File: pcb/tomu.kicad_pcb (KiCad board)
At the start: 2 copper layers, 13.2 x 10 mm, 16 parts, among them P1 USART0, P2 DEBUG, P3 USB-PCB, P4 RESET_PAD, P5 5V_PAD, P6 3V_PAD, U1 EFM32HG309

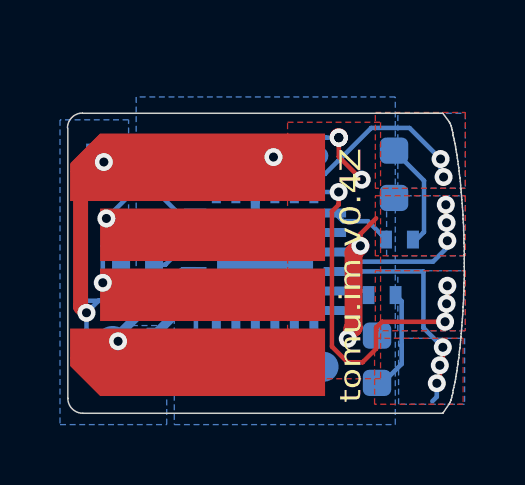
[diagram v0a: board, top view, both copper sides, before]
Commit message: eliminate edge.cut DRC
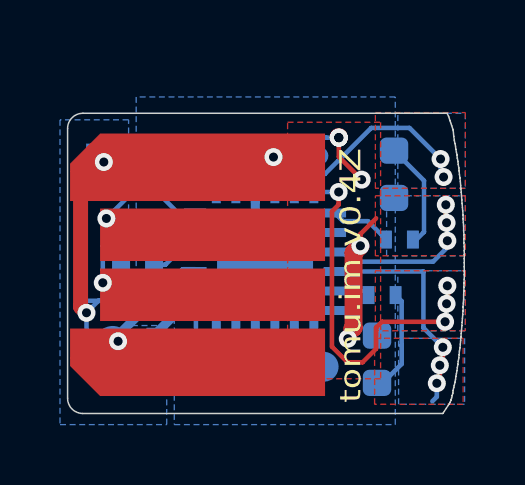
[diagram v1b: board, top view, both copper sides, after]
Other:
- outline, holes or cut-outs redrawn
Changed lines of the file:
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@@
 (kicad_pcb (version 20211014) (generator pcbnew)
   (general
-    (thickness 0.6)
+    (thickness 1.6)
   )
   (paper "User" 200 150.012)
@@
   )
   (setup
+    (stackup
+      (layer "F.SilkS" (type "Top Silk Screen"))
+      (layer "F.Paste" (type "Top Solder Paste"))
+      (layer "F.Mask" (type "Top Solder Mask") (thickness 0.01))
+      (layer "F.Cu" (type "copper") (thickness 0.035))
+      (layer "dielectric 1" (type "core") (thickness 1.51) (material "FR4") (epsilon_r 4.5) (loss_tangent 0.02))
+      (layer "B.Cu" (type "copper") (thickness 0.035))
+      (layer "B.Mask" (type "Bottom Solder Mask") (thickness 0.01))
+      (layer "B.Paste" (type "Bottom Solder Paste"))
+      (layer "B.SilkS" (type "Bottom Silk Screen"))
+      (copper_finish "None")
+      (dielectric_constraints no)
+    )
     (pad_to_mask_clearance 0.07)
     (solder_mask_min_width 0.07)
     (aux_axis_origin 17.025 26.5)
-    (grid_origin 29.12902 16.713447)
+    (grid_origin 29.717 16.8)
     (pcbplotparams
       (layerselection 0x00010fc_80000001)
@@
   (gr_line (start 29.95 17.05) (end 18.95 17.05) (layer "Dwgs.User") (width 0.1))
   (gr_line (start 18.95 26.05) (end 29.95 26.05) (layer "Dwgs.User") (width 0.1))
-  (gr_arc (start 17.012461 17.292697) (mid 17.158908 16.939144) (end 17.512461 16.792697) (layer "Edge.Cuts") (width 0.05))
-  (gr_line (start 29.888221 17.626525) (end 29.868221 17.536525) (layer "Edge.Cuts") (width 0.05))
   (gr_line (start 30.198221 20.316525) (end 30.198221 20.186525) (layer "Edge.Cuts") (width 0.05))
-  (gr_line (start 29.908221 17.706525) (end 29.888221 17.626525) (layer "Edge.Cuts") (width 0.05))
+  (gr_line locked (start 29.908221 17.706525) (end 29.888221 17.562) (layer "Edge.Cuts") (width 0.05))
   (gr_line (start 29.958221 17.996525) (end 29.948221 17.896525) (layer "Edge.Cuts") (width 0.05))
   (gr_line (start 30.218221 22.856525) (end 30.228221 22.726525) (layer "Edge.Cuts") (width 0.05))
   (gr_line (start 30.228221 22.726525) (end 30.228221 22.596525) (layer "Edge.Cuts") (width 0.05))
   (gr_line (start 29.868221 26.036525) (end 29.888221 25.946525) (layer "Edge.Cuts") (width 0.05))
+  (gr_arc (start 17.017 17.308) (mid 17.16579 16.94879) (end 17.525001 16.8) (layer "Edge.Cuts") (width 0.05))
   (gr_line (start 30.028221 18.406525) (end 30.008221 18.296525) (layer "Edge.Cuts") (width 0.05))
   (gr_line (start 30.218221 20.716525) (end 30.218221 20.576525) (layer "Edge.Cuts") (width 0.05))
   (gr_line (start 30.108221 24.496525) (end 30.118221 24.376525) (layer "Edge.Cuts") (width 0.05))
+  (gr_line (start 29.8186 17.2064) (end 29.7678 17.054) (layer "Edge.Cuts") (width 0.05))
   (gr_line (start 30.208221 23.126525) (end 30.218221 22.996525) (layer "Edge.Cuts") (width 0.05))
   (gr_line (start 30.228221 20.846525) (end 30.218221 20.716525) (layer "Edge.Cuts") (width 0.05))
-  (gr_line (start 29.868221 17.536525) (end 29.858221 17.446525) (layer "Edge.Cuts") (width 0.05))
-  (gr_line (start 17.025 17.3) (end 17.025 26.3) (layer "Edge.Cuts") (width 0.05))
   (gr_line (start 30.188221 23.516525) (end 30.198221 23.386525) (layer "Edge.Cuts") (width 0.05))
   (gr_line (start 30.068221 18.726525) (end 30.058221 18.616525) (layer "Edge.Cuts") (width 0.05))
+  (gr_line (start 29.717 16.9016) (end 29.6662 16.8) (layer "Edge.Cuts") (width 0.05))
   (gr_line (start 30.188221 20.056525) (end 30.178221 19.936525) (layer "Edge.Cuts") (width 0.05))
   (gr_line (start 30.218221 20.576525) (end 30.208221 20.446525) (layer "Edge.Cuts") (width 0.05))
+  (gr_line (start 17.017 17.308006) (end 17.017 26.300006) (layer "Edge.Cuts") (width 0.05))
   (gr_line (start 29.978221 25.476525) (end 29.998221 25.376525) (layer "Edge.Cuts") (width 0.05))
   (gr_line (start 29.978221 18.096525) (end 29.958221 17.996525) (layer "Edge.Cuts") (width 0.05))
   (gr_line (start 30.228221 22.456525) (end 30.238221 22.326525) (layer "Edge.Cuts") (width 0.05))
   (gr_line (start 30.198221 23.386525) (end 30.198221 23.256525) (layer "Edge.Cuts") (width 0.05))
+  (gr_line (start 29.7678 17.054) (end 29.717 16.9016) (layer "Edge.Cuts") (width 0.05))
   (gr_line (start 29.798221 26.356525) (end 29.818221 26.286525) (layer "Edge.Cuts") (width 0.05))
   (gr_line (start 29.838221 26.206525) (end 29.858221 26.126525) (layer "Edge.Cuts") (width 0.05))
-  (gr_line (start 29.838221 17.366525) (end 29.818221 17.286525) (layer "Edge.Cuts") (width 0.05))
   (gr_line (start 29.768221 26.436525) (end 29.798221 26.356525) (layer "Edge.Cuts") (width 0.05))
   (gr_line (start 30.078221 24.726525) (end 30.098221 24.616525) (layer "Edge.Cuts") (width 0.05))
   (gr_line (start 30.228221 20.976525) (end 30.228221 20.846525) (layer "Edge.Cuts") (width 0.05))
-  (gr_line (start 29.818221 17.286525) (end 29.798221 17.216525) (layer "Edge.Cuts") (width 0.05))
   (gr_line (start 30.158221 19.686525) (end 30.148221 19.556525) (layer "Edge.Cuts") (width 0.05))
   (gr_line (start 30.138221 19.436525) (end 30.128221 19.316525) (layer "Edge.Cuts") (width 0.05))
@@
   (gr_line (start 30.008221 18.296525) (end 29.998221 18.196525) (layer "Edge.Cuts") (width 0.05))
   (gr_line (start 30.238221 22.056525) (end 30.238221 21.916525) (layer "Edge.Cuts") (width 0.05))
-  (gr_line (start 29.525 16.8) (end 29.738221 17.086525) (layer "Edge.Cuts") (width 0.05))
-  (gr_line (start 29.525 26.8) (end 29.738221 26.486525) (layer "Edge.Cuts") (width 0.05))
+  (gr_line (start 29.888221 17.562) (end 29.8694 17.3588) (layer "Edge.Cuts") (width 0.05))
+  (gr_line (start 29.525 26.8076) (end 29.738221 26.486525) (layer "Edge.Cuts") (width 0.05))
   (gr_line (start 30.228221 21.116525) (end 30.228221 20.976525) (layer "Edge.Cuts") (width 0.05))
   (gr_line (start 29.998221 18.196525) (end 29.978221 18.096525) (layer "Edge.Cuts") (width 0.05))
@@
   (gr_line (start 30.238221 21.916525) (end 30.238221 21.786525) (layer "Edge.Cuts") (width 0.05))
   (gr_line (start 29.888221 25.946525) (end 29.908221 25.866525) (layer "Edge.Cuts") (width 0.05))
+  (gr_line (start 29.8694 17.3588) (end 29.8186 17.2064) (layer "Edge.Cuts") (width 0.05))
   (gr_line (start 30.068221 24.846525) (end 30.078221 24.726525) (layer "Edge.Cuts") (width 0.05))
   (gr_line (start 30.078221 18.846525) (end 30.068221 18.726525) (layer "Edge.Cuts") (width 0.05))
-  (gr_arc (start 17.525 26.8) (mid 17.171447 26.653553) (end 17.025 26.3) (layer "Edge.Cuts") (width 0.05))
   (gr_line (start 29.958221 25.576525) (end 29.978221 25.476525) (layer "Edge.Cuts") (width 0.05))
-  (gr_line (start 29.768221 17.136525) (end 29.738221 17.086525) (layer "Edge.Cuts") (width 0.05))
+  (gr_line (start 17.525 16.8) (end 29.6662 16.8) (layer "Edge.Cuts") (width 0.05))
   (gr_line (start 30.178221 23.636525) (end 30.188221 23.516525) (layer "Edge.Cuts") (width 0.05))
   (gr_line (start 30.108221 19.076525) (end 30.098221 18.956525) (layer "Edge.Cuts") (width 0.05))
@@
   (gr_line (start 30.218221 22.996525) (end 30.218221 22.856525) (layer "Edge.Cuts") (width 0.05))
   (gr_line (start 29.818221 26.286525) (end 29.838221 26.206525) (layer "Edge.Cuts") (width 0.05))
-  (gr_line (start 29.858221 17.446525) (end 29.838221 17.366525) (layer "Edge.Cuts") (width 0.05))
   (gr_line (start 30.118221 19.196525) (end 30.108221 19.076525) (layer "Edge.Cuts") (width 0.05))
   (gr_line (start 29.928221 17.806525) (end 29.908221 17.706525) (layer "Edge.Cuts") (width 0.05))
@@
   (gr_line (start 29.858221 26.126525) (end 29.868221 26.036525) (layer "Edge.Cuts") (width 0.05))
   (gr_line (start 30.148221 24.016525) (end 30.158221 23.886525) (layer "Edge.Cuts") (width 0.05))
+  (gr_line (start 17.525 26.8076) (end 29.525 26.8076) (layer "Edge.Cuts") (width 0.05))
   (gr_line (start 30.118221 24.376525) (end 30.128221 24.256525) (layer "Edge.Cuts") (width 0.05))
-  (gr_line (start 17.525 26.8) (end 29.525 26.8) (layer "Edge.Cuts") (width 0.05))
+  (gr_arc (start 17.525 26.8076) (mid 17.165874 26.659013) (end 17.017 26.300006) (layer "Edge.Cuts") (width 0.05))
   (gr_line (start 30.228221 22.596525) (end 30.228221 22.456525) (layer "Edge.Cuts") (width 0.05))
   (gr_line (start 30.238221 21.386525) (end 30.238221 21.246525) (layer "Edge.Cuts") (width 0.05))
@@
   (gr_line (start 30.238221 22.186525) (end 30.238221 22.056525) (layer "Edge.Cuts") (width 0.05))
   (gr_line (start 30.148221 19.556525) (end 30.138221 19.436525) (layer "Edge.Cuts") (width 0.05))
-  (gr_line (start 29.798221 17.216525) (end 29.768221 17.136525) (layer "Edge.Cuts") (width 0.05))
   (gr_line (start 30.098221 18.956525) (end 30.078221 18.846525) (layer "Edge.Cuts") (width 0.05))
   (gr_line (start 30.098221 24.616525) (end 30.108221 24.496525) (layer "Edge.Cuts") (width 0.05))
@@
   (gr_line (start 30.058221 18.616525) (end 30.038221 18.506525) (layer "Edge.Cuts") (width 0.05))
   (gr_line (start 30.028221 25.166525) (end 30.038221 25.066525) (layer "Edge.Cuts") (width 0.05))
-  (gr_line (start 29.525 16.8) (end 17.525 16.8) (layer "Edge.Cuts") (width 0.05))
   (gr_text "T" (at 24.56 25.96) (layer "B.SilkS")
     (effects (font (size 0.6 0.6) (thickness 0.15)) (justify mirror))
